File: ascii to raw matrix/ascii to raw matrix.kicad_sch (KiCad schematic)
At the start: 38 parts, among them J1 Conn_01x02_Pin, J10 parallel ascii, J11 apple 2e platinum, J2 Conn_01x02_Pin, J3 Conn_01x02_Pin, J4 Conn_01x02_Pin, J5 invert strobe, J6 invert busy, J7 reset, J8 power in, J9 parallel ascii, U1 74LS138, U2 74LS86, U3 74AHCT595, U4 74HCT597, U5 74HCT597, U6 Arduino Pro Mini, U7 L7805

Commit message: cleaned up for fab
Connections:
- no-connect marks 24 -> 25
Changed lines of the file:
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@@
   (no_connect (at 88.265 148.59))
   (no_connect (at 88.265 156.21))
+  (no_connect (at 98.425 89.535))
   (no_connect (at 88.265 179.07))
   (no_connect (at 75.565 171.45))

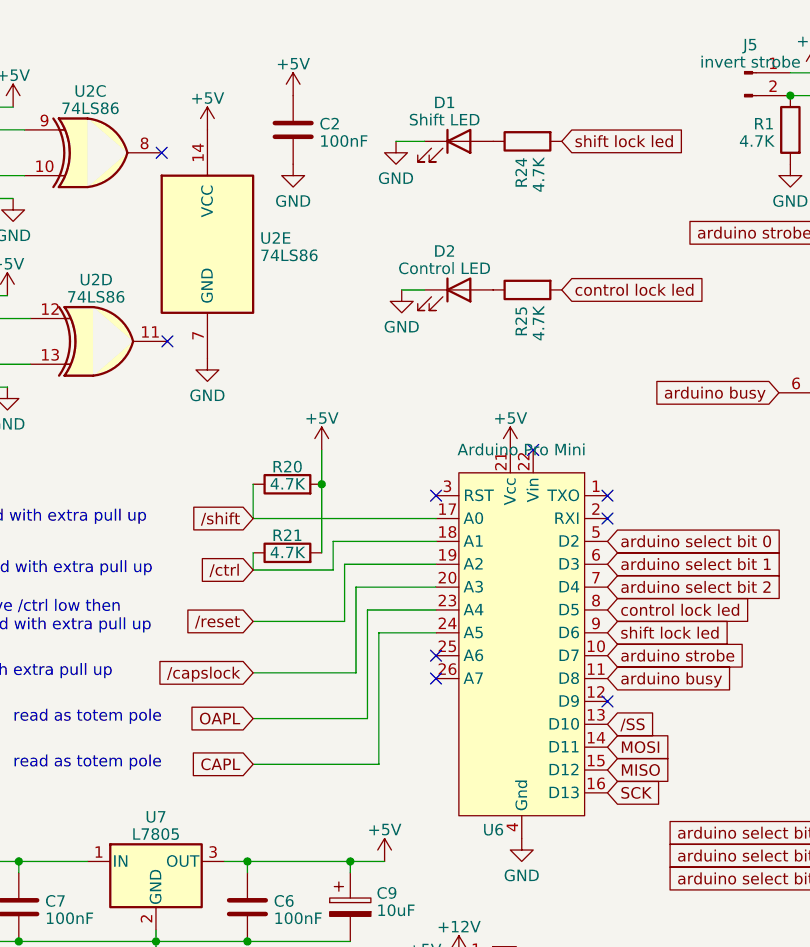
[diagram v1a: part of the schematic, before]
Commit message: tweaked values for resistors to be more reasonable
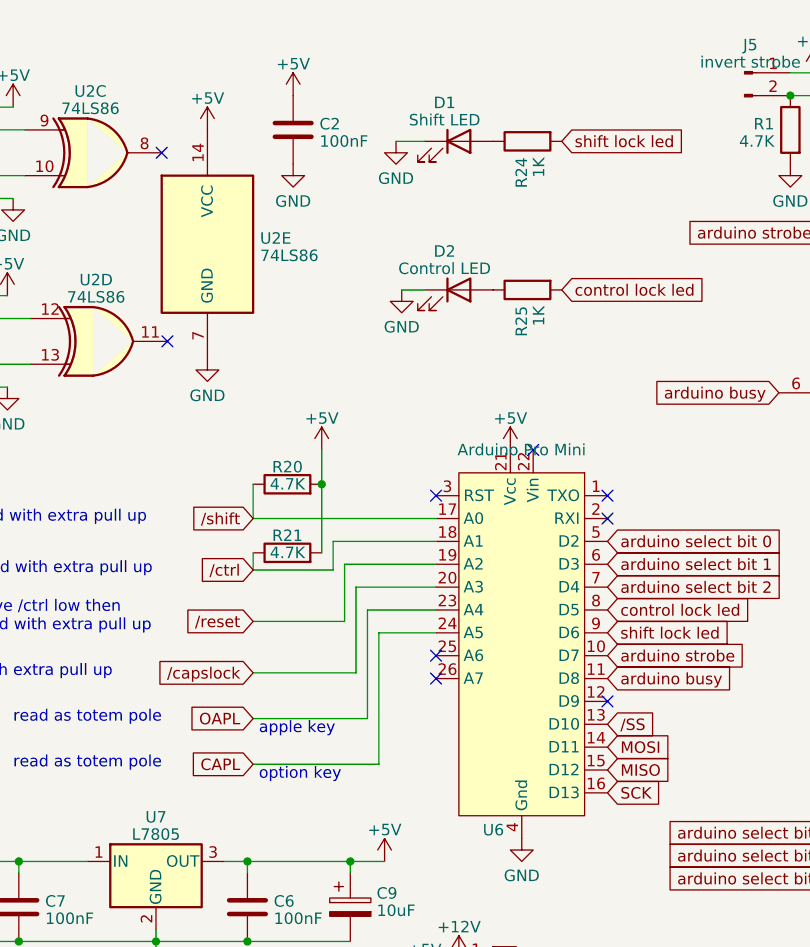
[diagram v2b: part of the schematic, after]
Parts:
- R24, R25: value 4.7K -> 1K
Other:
- note added: "apple key"
- note added: "option key"
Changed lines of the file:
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@@
+    (effects (font (size 1.27 1.27)) (justify left bottom))
+  )
+  (text "option key" (at 59.69 98.425 0)
+    (effects (font (size 1.27 1.27)) (justify left bottom))
+  )
+  (text "apple key" (at 59.69 93.345 0)
     (effects (font (size 1.27 1.27)) (justify left bottom))
   )
@@
       (effects (font (size 1.27 1.27)) (justify left))
     )
-    (property "Value" "4.7K" (at 90.8123 29.083 0)
+    (property "Value" "1K" (at 90.8123 29.083 0)
       (effects (font (size 1.27 1.27)) (justify left))
     )
@@
       (effects (font (size 1.27 1.27)) (justify left))
     )
-    (property "Value" "4.7K" (at 90.8123 45.593 0)
-      (effects (font (size 1.27 1.27)) (justify left))
-    )
+    (property "Value" "1K" (at 90.8123 45.593 0)
+      (effects (font (size 1.27 1.27)) (justify left))
+    )
